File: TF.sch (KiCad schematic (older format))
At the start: 6 parts

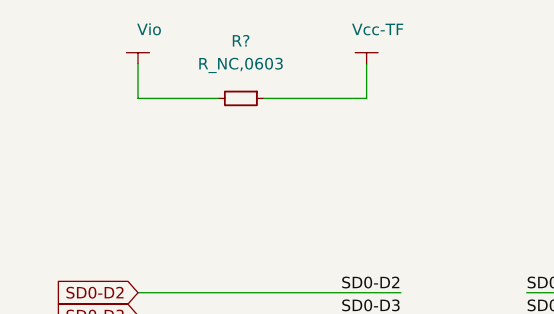
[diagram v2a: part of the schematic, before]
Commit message: update Vio -> VCC-IO,
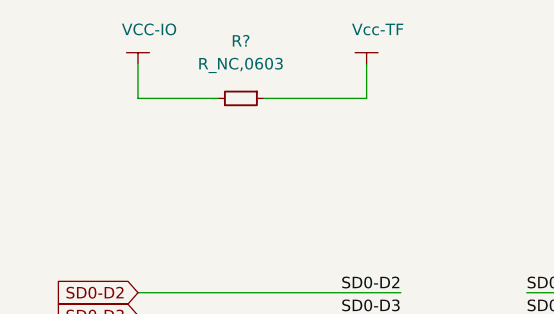
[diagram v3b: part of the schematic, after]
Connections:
- net Vio renamed VCC-IO
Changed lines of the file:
@@
 	6350 4100 7400 4100
-$Comp
-L taobao-components:Vio #PWR?
-U 1 1 5C272DF7
-P 3600 2900
-F 0 "#PWR?" H 3600 2750 50  0001 C CNN
-F 1 "Vio" H 3650 3050 50  0000 C CNN
-F 2 "" H 3600 2900 50  0001 C CNN
-F 3 "" H 3600 2900 50  0001 C CNN
-	1    3600 2900
-	1    0    0    -1
-$EndComp
 $Comp
 L taobao-components:Vcc-TF #PWR?
@@
 Wire Wire Line
 	4600 3050 4600 2900
+$Comp
+L taobao-components:VCC-IO #PWR?
+U 1 1 5C7DEB10
+P 3600 2900
+F 0 "#PWR?" H 3600 2750 50  0001 C CNN
+F 1 "VCC-IO" H 3650 3050 50  0000 C CNN
+F 2 "" H 3600 2900 50  0001 C CNN
+F 3 "" H 3600 2900 50  0001 C CNN
+	1    3600 2900
+	1    0    0    -1
+$EndComp
 $EndSCHEMATC
